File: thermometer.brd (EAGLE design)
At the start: 101.6 x 50.8 mm, 17 parts, among them IC1 MPQ3906, IC2 MPQ3904, IC4 CD4066BE, IC5 LM311N, IC6 LM324N

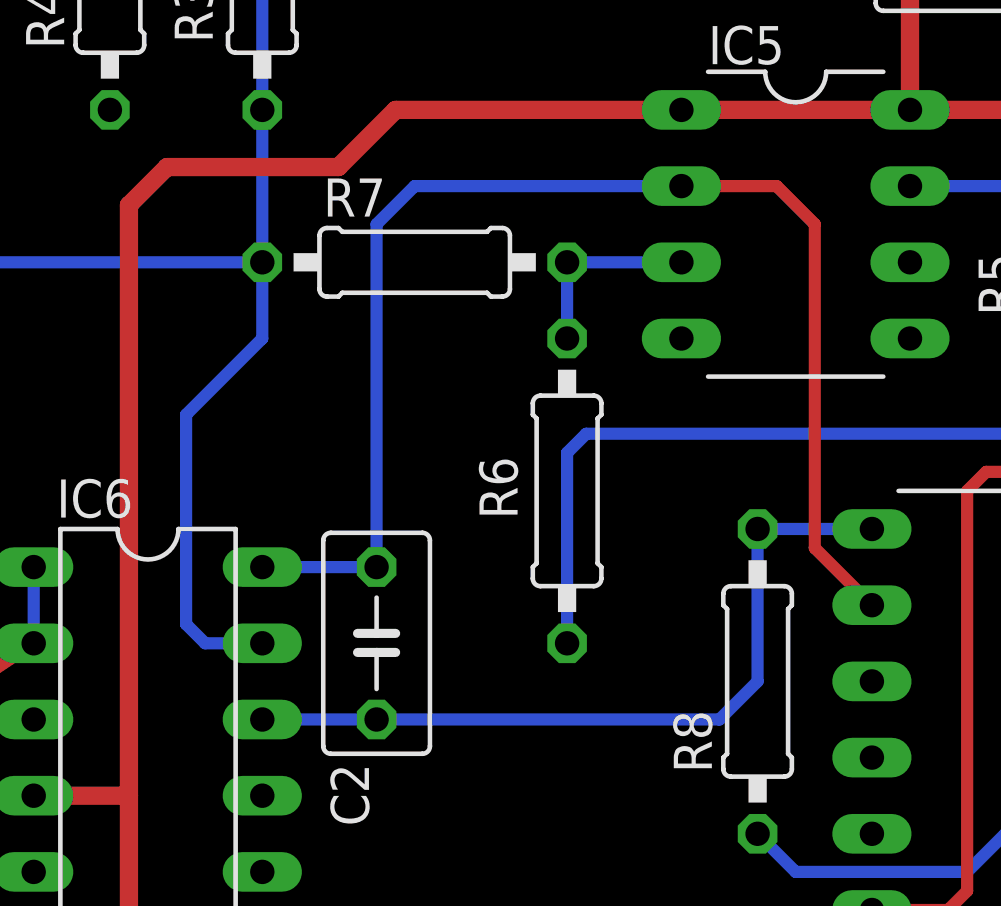
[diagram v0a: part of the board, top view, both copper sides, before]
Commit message: fixed in+ and in- pins of op amps and comparator
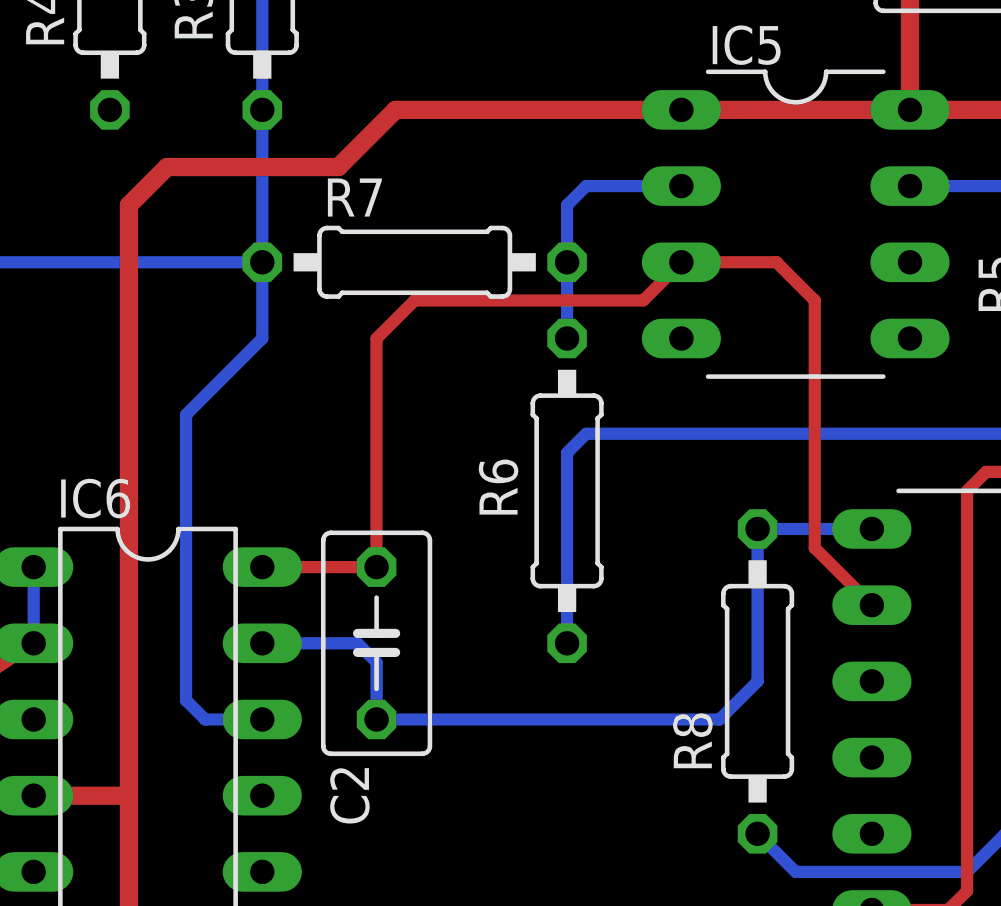
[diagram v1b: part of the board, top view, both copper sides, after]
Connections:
- net INTEGRATOR_IN: now also IC6.13; no longer IC6.12
- net INTEGRATOR_OUT: now also IC5.3; no longer IC5.2
- net V+: now also IC6.12; no longer IC6.13
- net V_HYSTERESIS: now also IC5.2; no longer IC5.3
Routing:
- net INTEGRATOR_OUT: track 44.4 -> 38.6 mm
- net V+: track 87.9 -> 90.4 mm
- net V_HYSTERESIS: track 6.35 -> 8.52 mm
- net INTEGRATOR_IN: track 25.9 -> 28.1 mm
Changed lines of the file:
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@@
 <contactref element="IC3" pad="2"/>
 <contactref element="R7" pad="1"/>
-<contactref element="IC6" pad="13"/>
 <wire x1="43.815" y1="31.115" x2="43.815" y2="36.195" width="0.4064" layer="16"/>
 <wire x1="43.815" y1="36.195" x2="43.815" y2="42.545" width="0.4064" layer="16"/>
@@
 <wire x1="28.575" y1="19.05" x2="26.67" y2="17.145" width="0.4064" layer="1"/>
 <wire x1="26.67" y1="17.145" x2="15.875" y2="17.145" width="0.4064" layer="1"/>
-<wire x1="43.815" y1="18.415" x2="41.91" y2="18.415" width="0.4064" layer="16"/>
-<wire x1="41.91" y1="18.415" x2="41.275" y2="19.05" width="0.4064" layer="16"/>
-<wire x1="41.275" y1="19.05" x2="41.275" y2="26.035" width="0.4064" layer="16"/>
+<wire x1="41.275" y1="16.51" x2="41.275" y2="26.035" width="0.4064" layer="16"/>
 <wire x1="41.275" y1="26.035" x2="43.815" y2="28.575" width="0.4064" layer="16"/>
 <wire x1="43.815" y1="28.575" x2="43.815" y2="31.115" width="0.4064" layer="16"/>
@@
 <vertex x="17.78" y="18.415"/>
 </polygon>
+<contactref element="IC6" pad="12"/>
+<wire x1="41.275" y1="16.51" x2="41.91" y2="15.875" width="0.4064" layer="16"/>
+<wire x1="41.91" y1="15.875" x2="43.815" y2="15.875" width="0.4064" layer="16"/>
+<wire x1="15.875" y1="12.065" x2="15.875" y2="17.145" width="0" layer="19" extent="1-1"/>
+<wire x1="8.255" y1="17.145" x2="15.875" y2="17.145" width="0" layer="19" extent="1-1"/>
+<wire x1="8.255" y1="12.065" x2="8.255" y2="17.145" width="0" layer="19" extent="1-1"/>
 </signal>
 <signal name="GND">
@@
 <contactref element="R7" pad="2"/>
 <contactref element="R6" pad="1"/>
-<contactref element="IC5" pad="3"/>
 <wire x1="53.975" y1="31.115" x2="53.975" y2="28.575" width="0.4064" layer="16"/>
-<wire x1="53.975" y1="31.115" x2="57.785" y2="31.115" width="0.4064" layer="16"/>
+<contactref element="IC5" pad="2"/>
+<wire x1="53.975" y1="31.115" x2="53.975" y2="33.02" width="0.4064" layer="16"/>
+<wire x1="53.975" y1="33.02" x2="54.61" y2="33.655" width="0.4064" layer="16"/>
+<wire x1="54.61" y1="33.655" x2="57.785" y2="33.655" width="0.4064" layer="16"/>
 </signal>
 <signal name="-V_IN">
@@
 <contactref element="C2" pad="1"/>
 <contactref element="IC4" pad="8"/>
-<contactref element="IC6" pad="12"/>
-<wire x1="43.815" y1="15.875" x2="47.625" y2="15.875" width="0.4064" layer="16"/>
 <wire x1="47.625" y1="15.875" x2="59.055" y2="15.875" width="0.4064" layer="16"/>
 <wire x1="59.055" y1="15.875" x2="60.325" y2="17.145" width="0.4064" layer="16"/>
 <wire x1="60.325" y1="17.145" x2="60.325" y2="22.225" width="0.4064" layer="16"/>
 <wire x1="60.325" y1="22.225" x2="64.135" y2="22.225" width="0.4064" layer="16"/>
+<contactref element="IC6" pad="13"/>
+<wire x1="47.625" y1="15.875" x2="47.625" y2="17.78" width="0.4064" layer="16"/>
+<wire x1="47.625" y1="17.78" x2="46.99" y2="18.415" width="0.4064" layer="16"/>
+<wire x1="46.99" y1="18.415" x2="43.815" y2="18.415" width="0.4064" layer="16"/>
 </signal>
 <signal name="INTEGRATOR_OUT">
 <contactref element="C2" pad="2"/>
 <contactref element="IC4" pad="9"/>
-<contactref element="IC5" pad="2"/>
+<wire x1="64.135" y1="19.685" x2="62.23" y2="21.59" width="0.4064" layer="1"/>
 <contactref element="IC6" pad="14"/>
-<wire x1="43.815" y1="20.955" x2="47.625" y2="20.955" width="0.4064" layer="16"/>
-<wire x1="64.135" y1="19.685" x2="62.23" y2="21.59" width="0.4064" layer="1"/>
-<wire x1="62.23" y1="21.59" x2="62.23" y2="32.385" width="0.4064" layer="1"/>
-<wire x1="62.23" y1="32.385" x2="60.96" y2="33.655" width="0.4064" layer="1"/>
-<wire x1="60.96" y1="33.655" x2="57.785" y2="33.655" width="0.4064" layer="1"/>
-<wire x1="57.785" y1="33.655" x2="48.895" y2="33.655" width="0.4064" layer="16"/>
-<wire x1="48.895" y1="33.655" x2="47.625" y2="32.385" width="0.4064" layer="16"/>
-<wire x1="47.625" y1="32.385" x2="47.625" y2="20.955" width="0.4064" layer="16"/>
+<contactref element="IC5" pad="3"/>
+<wire x1="62.23" y1="21.59" x2="62.23" y2="29.845" width="0.4064" layer="1"/>
+<wire x1="62.23" y1="29.845" x2="60.96" y2="31.115" width="0.4064" layer="1"/>
+<wire x1="60.96" y1="31.115" x2="57.785" y2="31.115" width="0.4064" layer="1"/>
+<wire x1="47.625" y1="20.955" x2="43.815" y2="20.955" width="0.4064" layer="1"/>
+<wire x1="47.625" y1="20.955" x2="47.625" y2="28.575" width="0.4064" layer="1"/>
+<wire x1="47.625" y1="28.575" x2="48.895" y2="29.845" width="0.4064" layer="1"/>
+<wire x1="48.895" y1="29.845" x2="56.515" y2="29.845" width="0.4064" layer="1"/>
+<wire x1="56.515" y1="29.845" x2="57.785" y2="31.115" width="0.4064" layer="1"/>
 </signal>
 <signal name="+3V3">

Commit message: fixed labelling
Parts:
- IC6: value LM324N -> LM6134
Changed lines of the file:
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@@
 <element name="IC4" library="6301-temp-sensor-rev1" package="DIL14" value="CD4066BE" x="67.945" y="14.605" rot="R90"/>
 <element name="IC5" library="6301-temp-sensor-rev1" package="DIL08" value="LM311N" x="61.595" y="32.385" rot="R270"/>
-<element name="IC6" library="linear" package="DIL14" value="LM324N" x="40.005" y="13.335" rot="R270"/>
+<element name="IC6" library="linear" package="DIL14" value="LM6134" x="40.005" y="13.335" rot="R270"/>
 <element name="R1" library="rcl" package="0207/10" value="510" x="32.385" y="20.955" smashed="yes" rot="R90">
 <attribute name="NAME" x="30.861" y="17.907" size="1.27" layer="25" ratio="10" rot="R90"/>
